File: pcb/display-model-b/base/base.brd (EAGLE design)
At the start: 121.9 x 17.8 mm, 41 parts, among them J1 SNG-2MM-HEADER-07-V, Q1 MMBT3904, Q2 MMBT3904, Q3 MMBT3904, Q4 MMBT3904, U1 PCA9634PW, U2 TSL2561FN, X1 CLOCK_LED_SEGMENT, X2 CLOCK_LED_SEGMENT, X3 CLOCK_LED_SEGMENT, X4 CLOCK_LED_SEGMENT, X5 CLOCK_LED_DOTS

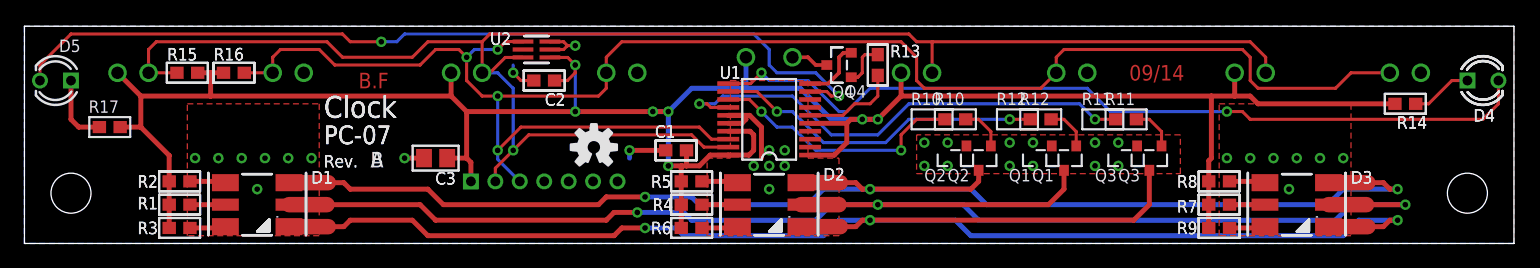
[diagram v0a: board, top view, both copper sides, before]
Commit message: Corrected drawings of touch panel PCB
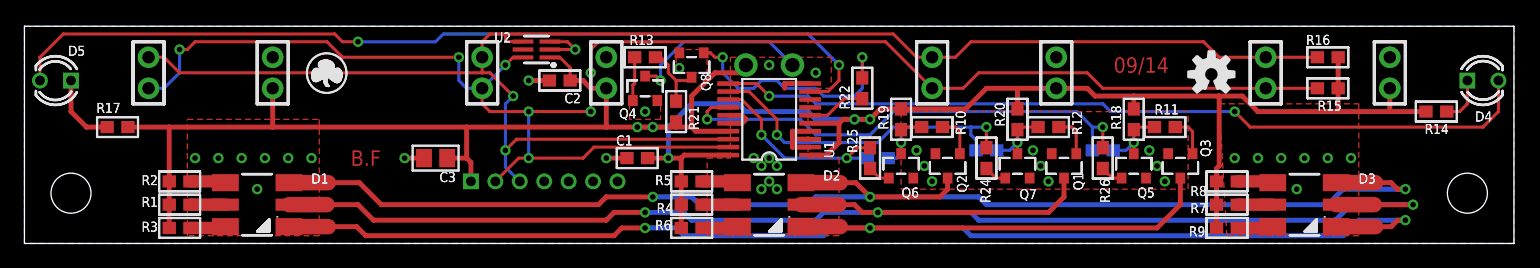
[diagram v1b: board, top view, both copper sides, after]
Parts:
- added Q5, Q6, Q7, Q8: MMBT3904, Transistor:SOT23
- added R18, R19, R20, R21, R22, R24, R25, R26: 10k, Passive:SMD_0603
- added R23, R27, R28: N/A, Passive:SMD_0603
- added U$2: (no value), Symbols:LOGO2
- R10, R11, R12: value 2.2k -> 1k
- R13: value 3k -> 1k
- moved R15 93.4 mm to (106.7, 12.7)
- moved R16 89.5 mm to (106.7, 15.2), turned to 0 degrees
- moved U$3 50.9 mm to (97.2, 13.8)
- moved R13 19.1 mm to (50.8, 15.2), turned to 180 degrees
- moved Q4 16.0 mm to (50.8, 12.7), turned to 0 degrees
- moved U$5 6.38 mm to (27.9, 6.99)
- moved U$4 4.57 mm to (25.0, 8.76), flipped to the bottom
- moved C1 3.24 mm to (50.2, 6.99)
- moved R11 3.24 mm to (93.3, 9.53)
- moved Q2 2.62 mm to (75.6, 6.35)
- moved Q3 2.62 mm to (94.6, 6.35)
- moved R14 2.62 mm to (115.6, 10.8)
- moved R10 2.01 mm to (74.3, 9.53)
- moved U$1 1.42 mm to (89.2, 14.0)
- moved C2 1.27 mm to (43.8, 13.3)
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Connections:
- new net N$22: Q6.3, R10.1, R19.1, R23.2
- new net N$23: Q5.3, R11.1, R18.1, R27.2
- new net N$24: Q7.3, R12.1, R20.1, R28.2
- new net N$25: Q5.1, R26.1
- new net N$26: Q8.3, R13.1, R21.1
- new net N$27: Q8.1, R22.2
- new net N$28: Q6.1, R25.1
- new net N$30: Q7.1, R24.1
- net 3.3V: now also R18.2, R19.2, R20.2, R21.2
- net BL_BLUE: now also R26.2, R27.1; no longer R11.1
- net BL_GREEN: now also R23.1, R25.2; no longer R10.1
- net BL_RED: now also R24.2, R28.1; no longer R12.1
- net DOTS: now also R22.1; no longer R13.1
- net GND: now also Q5.2, Q6.2, Q7.2, Q8.2
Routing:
- net N$27: track 0.00 -> 20.2 mm, vias 0 -> 2
- net N$15: track 3.07 -> 15.1 mm, vias 0 -> 1
- net SCL: track 143.0 -> 132.6 mm, vias 4 -> 2
- net N$26: track 0.00 -> 6.08 mm
- net N$22: track 0.00 -> 5.98 mm, vias 0 -> 1
- net N$23: track 0.00 -> 5.82 mm, vias 0 -> 1
- net N$24: track 0.00 -> 5.82 mm, vias 0 -> 1
- net BL_GREEN: track 21.3 -> 16.4 mm
- net GND: track 25.5 -> 20.6 mm, vias 36 -> 38
- net DOTS: track 8.10 -> 4.84 mm
- net N$5: track 115.4 -> 113.2 mm
- net N$25: track 0.00 -> 1.87 mm
- net N$30: track 0.00 -> 1.87 mm
- net N$28: track 0.00 -> 1.87 mm
- net N$6: track 131.5 -> 133.3 mm
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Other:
- board text added: "B"
- board text added: "D5"
- board text added: "Q5"
- board text added: "Q6"
- board text added: "Q7"
- board text added: "Q8"
- board text added: "R17"
- board text added: "R18"
- board text added: "R19"
- board text added: "R20"
- board text added: "R21"
- board text added: "R22"
- board text added: "R23"
- board text added: "R24"
- board text added: "R25"
- board text added: "R26"
- board text added: "R27"
- board text added: "R28"
- board text removed: "A"

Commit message: Display base pcb (rev C), Touch panel (rev B)
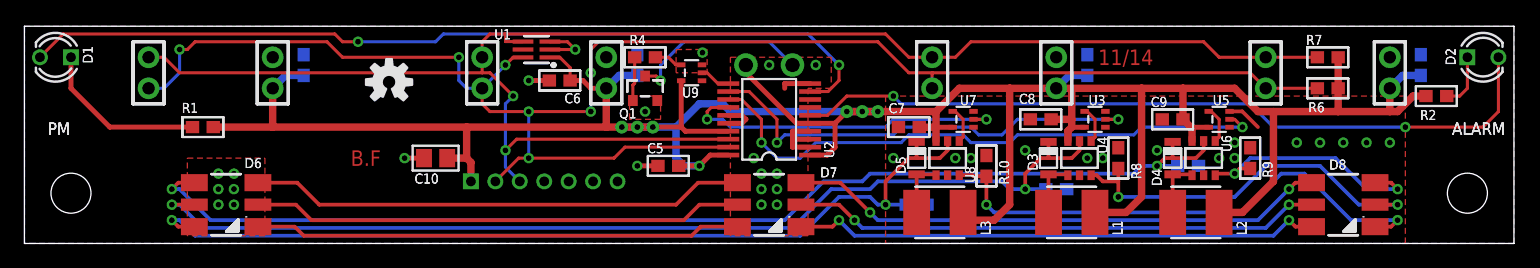
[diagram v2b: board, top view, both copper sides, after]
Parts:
- removed Q2, Q3, Q4, Q5, Q6, Q7, Q8: MMBT3904, Transistor:SOT23
- removed R11, R12, R13, R15, R16: 1k, Passive:SMD_0603
- removed R14, R17: 82, Passive:SMD_0603
- removed R18, R19, R20, R21, R22, R24, R25, R26: 10k, Passive:SMD_0603
- removed R23, R27, R28: N/A, Passive:SMD_0603
- removed R3, R5: 1, Passive:SMD_0603
- removed U$2: (no value), Symbols:LOGO2
- added C10: N/A, Passive:SMD_0805
- added C11, C12, C13, C4, C7, C8, C9: 1uF, Passive:SMD_0603
- added C5, C6: 100nF, Passive:SMD_0603
- added D6, D7, D8: SMP6-RGB, Optoelectronic:LED_RGB_PLCC6
- added L1, L2, L3: 22uH, Passive:IND-4X4
- added U3, U5, U7, U9: 74AHC1G04DCK, Logic:SC70-5
- added U4, U6, U8: AP5724W, IC:SOT23-6
- C1, C2: value 100nF -> 1uF
- C3: value N/A -> 1uF; device Passive:SMD_0805 -> Passive:SMD_0603
- D1, D2: value SMP6-RGB -> {ATTR:COLOR}; device Optoelectronic:LED_RGB_PLCC6 -> Optoelectronic:LED_3MM
- D3: value SMP6-RGB -> (none); device Optoelectronic:LED_RGB_PLCC6 -> Passive:SOD-323
- D4, D5: value {ATTR:COLOR} -> (none); device Optoelectronic:LED_3MM -> Passive:SOD-323
- R1: value 68 -> 82
- R10: value 1k -> 5.1 (0.5%)
- R2: value 1 -> 82
- R4: value 68 -> 3k
- R6: value 1 -> 1k
- R7: value 68 -> 1k
- R8, R9: value 1 -> 5.1 (0.5%)
- U1: value PCA9634PW -> TSL2561FN; device IC:TSSOP20 -> Optoelectronic:DFN-6
- U2: value TSL2561FN -> PCA9634PW; device Optoelectronic:DFN-6 -> IC:TSSOP20
- moved R2 103.1 mm to (115.6, 12.1), turned to 180 degrees
- moved D5 70.8 mm to (73.0, 6.99), turned to 90 degrees
- moved U$3 67.3 mm to (29.8, 13.2)
- moved D2 59.7 mm to (119.4, 15.2)
- moved C3 53.9 mm to (87.0, 14.6), flipped to the bottom, turned to 270 degrees
- moved R6 53.3 mm to (106.7, 12.7)
- moved Q1 34.9 mm to (50.8, 12.7), turned to 0 degrees
- moved C1 28.3 mm to (22.9, 14.6), flipped to the bottom, turned to 270 degrees
- moved D4 26.2 mm to (94.0, 6.99), turned to 90 degrees
- moved D3 21.3 mm to (83.8, 6.99), turned to 90 degrees
- moved D1 20.4 mm to (2.54, 15.2), turned to 180 degrees
- moved U1 19.9 mm to (41.9, 15.9), turned to 180 degrees
- moved U2 19.9 mm to (61.0, 10.2), turned to 90 degrees
- moved R7 14.6 mm to (106.7, 15.2)
- moved R4 12.7 mm to (50.8, 15.2), turned to 180 degrees
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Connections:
- removed net BL_BLUE: R26.2, R27.1, U1.14
- removed net BL_GREEN: R23.1, R25.2, U1.13
- removed net BL_RED: R24.2, R28.1, U1.12
- removed net N$11: D3.4, R7.2
- removed net N$13: Q2.1, R10.2
- removed net N$14: Q3.1, R11.2
- removed net N$17: Q1.1, R12.2
- removed net N$22: Q6.3, R10.1, R19.1, R23.2
- removed net N$23: Q5.3, R11.1, R18.1, R27.2
- removed net N$24: Q7.3, R12.1, R20.1, R28.2
- removed net N$27: Q8.1, R22.2
- removed net N$30: Q7.1, R24.1
- removed net N$7: D2.2, R5.2
- removed net N$9: D3.6, R9.2
- new net FB_B: D8.5, R10.2, U8.3
- new net FB_G: D8.1, R9.2, U6.3
- new net FB_R: D8.3, R8.2, U4.3
- new net N$29: U7.4, U8.4
- new net PWM_B: U2.14, U7.2
- new net PWM_G: U2.13, U5.2
- new net PWM_R: U2.12, U3.2
- new net SW_B: C13.1, D5.K, D6.6, U8.5
- new net SW_G: C11.1, D4.K, D6.2, U6.5
- new net SW_R: C12.1, D3.K, D6.4, U4.5
- net 3.3V: now also C1.2, C10.1, C3.2, C4.2, C5.1, C6.2, C7.2, C8.2, C9.2, L1.1, L2.1, L3.1, R1.2, R2.2, R6.2, R7.2, U2.17, U2.20, U2.5, U3.5, U4.6, U5.5, U6.6, U7.5, U8.6, U9.5; no longer C1.1, C3.1, R1.1, R14.2, R15.2, R16.2, R17.2, R18.2, R19.2, R2.1, R20.2, R21.2, R3.1, R4.1, R5.1, R6.1, R7.1, R8.1, R9.1, U1.17, U1.20, U1.5
- net DOTS: now also U2.11, U9.2; no longer R22.1, U1.6
- net GND: now also C1.1, C10.2, C11.2, C12.2, C13.2, C3.1, C4.1, C5.2, C6.1, C7.1, C8.1, C9.1, R10.1, R8.1, R9.1, U2.10, U2.15, U2.16, U2.4, U3.3, U4.2, U5.3, U6.2, U7.3, U8.2, U9.3; no longer C1.2, C3.2, Q2.2, Q3.2, Q4.2, Q5.2, Q6.2, Q7.2, Q8.2, U1.10, U1.15, U1.16, U1.4
- net N$1: now also D6.3, D7.4; no longer D1.2, R2.2
- net N$10: now also D4.A, L2.2, U6.1; no longer D3.2, R8.2
- net N$12: now also D5.A, L3.2, U8.1; no longer D1.3, D2.3, D3.3, Q1.3
- net N$15: now also Q1.3; no longer Q4.3
- net N$16: now also Q1.1, R4.2; no longer Q4.1, R13.2
- net N$18: now also D2.K, U2.6; no longer D4.K, U1.11
- net N$19: now also D2.A, R2.1; no longer D4.A, R14.1
- net N$2: now also D7.3, D8.4; no longer D1.4, R1.2
- net N$20: now also D1.A, R1.1; no longer D5.A, R17.1
- net N$21: now also D1.K, U2.9; no longer D5.K, U1.9
- net N$25: now also U3.4, U4.4; no longer Q5.1, R26.1
- net N$26: now also R4.1, U9.4; no longer Q8.3, R13.1, R21.1
- net N$28: now also U5.4, U6.4; no longer Q6.1, R25.1
- net N$3: now also D7.1, D8.2; no longer D1.6, R3.2
- net N$4: now also D6.1, D7.2; no longer D2.4, R4.2
- net N$5: now also D6.5, D7.6; no longer D1.1, D2.1, D3.1, Q2.3
- net N$6: now also D7.5, D8.6; no longer D1.5, D2.5, D3.5, Q3.3
- net N$8: now also D3.A, L1.2, U4.1; no longer D2.6, R6.2
- net SCL: now also R7.1, U1.4, U2.18; no longer R16.1, U1.18, U2.4
- net SDA: now also R6.1, U1.6, U2.19; no longer R15.1, U1.19, U2.6
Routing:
- net N$12: track 124.3 -> 4.78 mm, vias 3 -> 0
- net SW_G: track 0.00 -> 93.7 mm, vias 0 -> 2
- net N$6: track 133.3 -> 43.3 mm, vias 3 -> 2
- net SW_R: track 0.00 -> 84.6 mm, vias 0 -> 2
- net SW_B: track 0.00 -> 74.4 mm, vias 0 -> 2
- net N$5: track 113.2 -> 39.9 mm, vias 3 -> 0
- net PWM_G: track 0.00 -> 48.1 mm, vias 0 -> 2
- net FB_B: track 0.00 -> 43.5 mm, vias 0 -> 2
- net N$3: track 3.00 -> 44.3 mm, vias 0 -> 2
- net N$2: track 2.90 -> 43.4 mm, vias 0 -> 2
- net BL_BLUE: track 40.3 -> 0.00 mm, vias 2 -> 0
- net 3.3V: track 196.9 -> 237.1 mm, vias 5 -> 7
- net N$4: track 2.90 -> 40.7 mm
- net N$1: track 3.00 -> 40.3 mm
- net PWM_R: track 0.00 -> 37.1 mm, vias 0 -> 2
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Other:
- board text added: "ALARM"
- board text added: "C"
- board text added: "C10"
- board text added: "C11"
- board text added: "C12"
- board text added: "C13"
- board text added: "C4"
- board text added: "C5"
- board text added: "C6"
- board text added: "C7"
- board text added: "C8"
- board text added: "C9"
- board text added: "D6"
- board text added: "D7"
- board text added: "D8"
- board text added: "L1"
- board text added: "L2"
- board text added: "L3"
- board text added: "PM"
- board text added: "U3"
- board text added: "U4"
- board text added: "U5"
- board text added: "U6"
- board text added: "U7"
- board text added: "U8"
- board text added: "U9"
- board text removed: "B"
- board text removed: "Q2"
- board text removed: "Q3"
- board text removed: "Q4"
- board text removed: "Q5"
- board text removed: "Q6"
- board text removed: "Q7"
- board text removed: "Q8"
- board text removed: "R11"
- board text removed: "R12"
- board text removed: "R13"
- board text removed: "R14"
- board text removed: "R15"
- board text removed: "R16"
- board text removed: "R17"
- board text removed: "R18"
- board text removed: "R19"
- board text removed: "R20"
- board text removed: "R21"
- board text removed: "R22"
- board text removed: "R23"
- board text removed: "R24"
- board text removed: "R25"
- board text removed: "R26"
- board text removed: "R27"
- board text removed: "R28"
- board text removed: "R3"
- board text removed: "R5"
